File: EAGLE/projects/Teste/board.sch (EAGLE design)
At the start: 6 parts

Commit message: circuito de alimentacao pronto
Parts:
- added C2, C3, C7: (no value), rcl:CPOL-EUE5-6
- added C4, C5, C6: (no value), capacitor-wima:C5/3
- added IC1: 317T, linear:317T
- added IC2: 7805T, linear:7805T
- added JP3: (no value), pinhead:PINHD-1X2
- added R2, R3, R4, R5: (no value), rcl:R-US_0309/12
- added V1: 7408N, 74ttl-din:7408N
- C1: CAP (none) -> 100nF
- R1: SPICEPREFIX (none) -> 2K2
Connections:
- removed net VCC: C1.2, DIS1.VCC
- new net +3V3: C6.1, C7.+, IC1.VO, R2.2
- new net +5V: C1.2, C3.+, C5.1, DIS1.VCC, IC2.VO, JP2.2, R5.1, V1/1.A
- new net LCD_D4: DIS1.D4
- new net LCD_D5: DIS1.D5
- new net LCD_D6: DIS1.D6
- new net LCD_D7: DIS1.D7
- new net LCD_E: DIS1.E
- new net LCD_RS: DIS1.RS
- new net N$2: JP2.1, V1/1.Y
- new net N$3: C2.+, C4.1, IC1.VI, IC2.VI, JP3.2
- new net N$4: R2.1, R3.2
- new net N$5: IC1.ADJ, R3.1, R4.2
- new net N$6: DIS1.NC@1, R5.2
- net GND: now also C2.-, C3.-, C4.2, C5.2, C6.2, C7.-, DIS1.NC@2, DIS1.R/W, IC2.GND, JP2.3, JP3.1, R4.1
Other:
- moved on the sheet: JP1, JP2

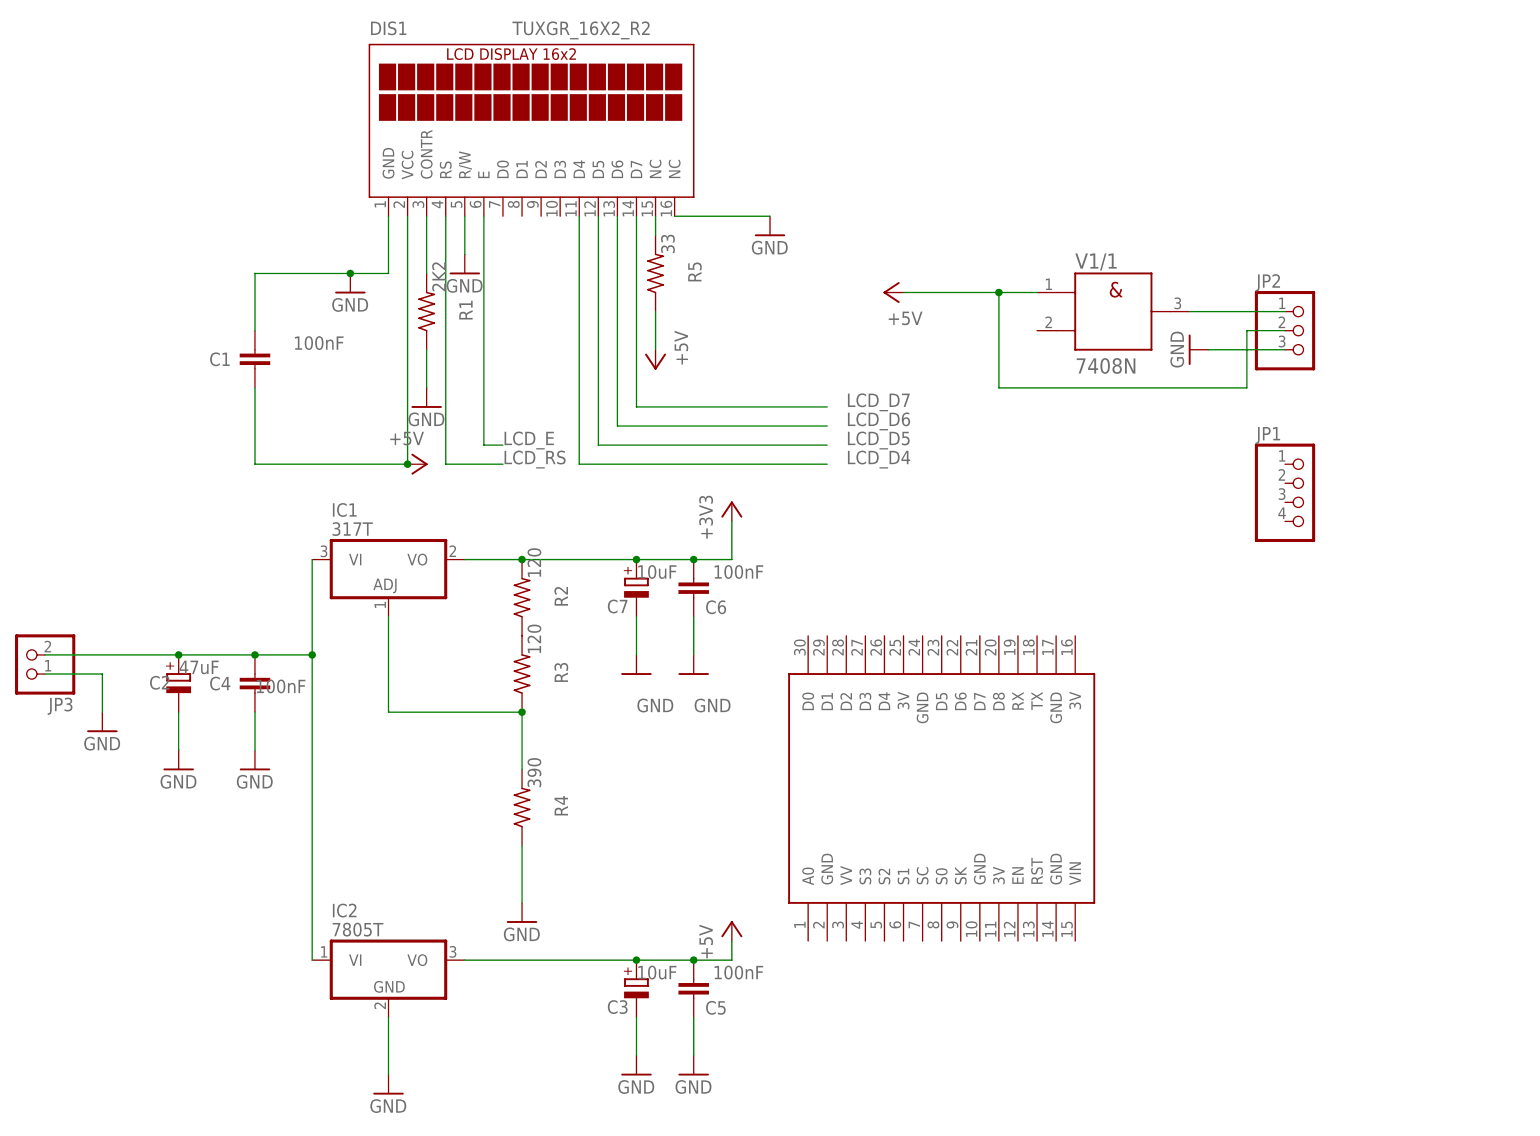
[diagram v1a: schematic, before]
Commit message: Fim do esquematico Inicio do roteamento
Ainda precisa corrigir alguns bugs no esquematico, ver com o benfica
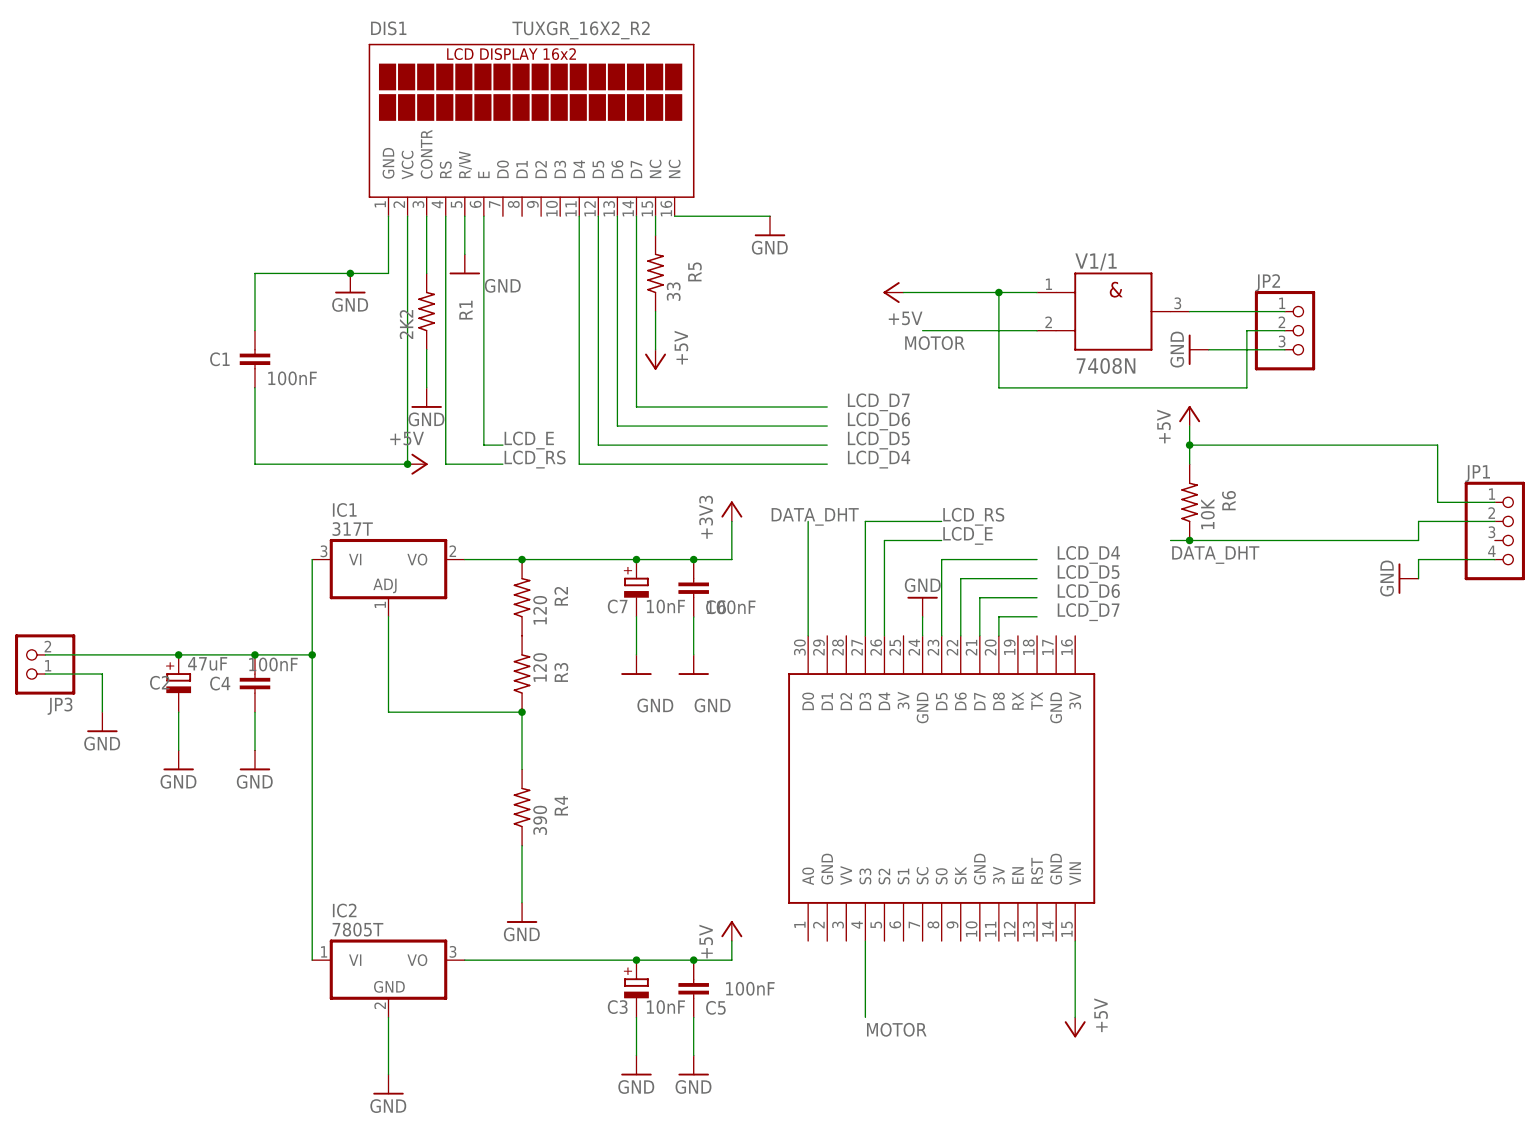
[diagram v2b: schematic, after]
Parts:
- added R6: 10K, rcl:R-US_0309/12
- C1, C4, C5, C6: value (none) -> 100nF
- C2: value (none) -> 47uF
- C3, C7: value (none) -> 10nF
- R1: value (none) -> 2K2
- R2, R3: value (none) -> 120
- R4: value (none) -> 390
- R5: value (none) -> 33
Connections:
- new net DATA_DHT: JP1.2, R6.1, U$1.D0
- new net MOTOR: U$1.S3, V1/1.B
- net +5V: now also JP1.1, R6.2, U$1.VIN
- net GND: now also JP1.4, U$1.GND@4
- net LCD_D4: now also U$1.D5
- net LCD_D5: now also U$1.D6
- net LCD_D6: now also U$1.D7
- net LCD_D7: now also U$1.D8
- net LCD_E: now also U$1.D4
- net LCD_RS: now also U$1.D3
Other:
- moved on the sheet: JP1
